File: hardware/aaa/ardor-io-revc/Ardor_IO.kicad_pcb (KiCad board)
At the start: 2 copper layers, 68 x 46 mm, 81 parts, among them J101 PI 40-PIN HEADER, J102 CODEC AUX L / GND / R, J202 TO MIDI PANEL / 4,5, J302 TO EXP PANEL / T,R,S, J502 TO YOUR AMP CIRCUIT, J503 TO LINE PANEL / T,S, K501 G5V-1 DC5, Q501 AO3400A, U201 H11L1M, U301 ADS1115IDGS, U401 TLV9002IDR, U402 TLV9002IDR

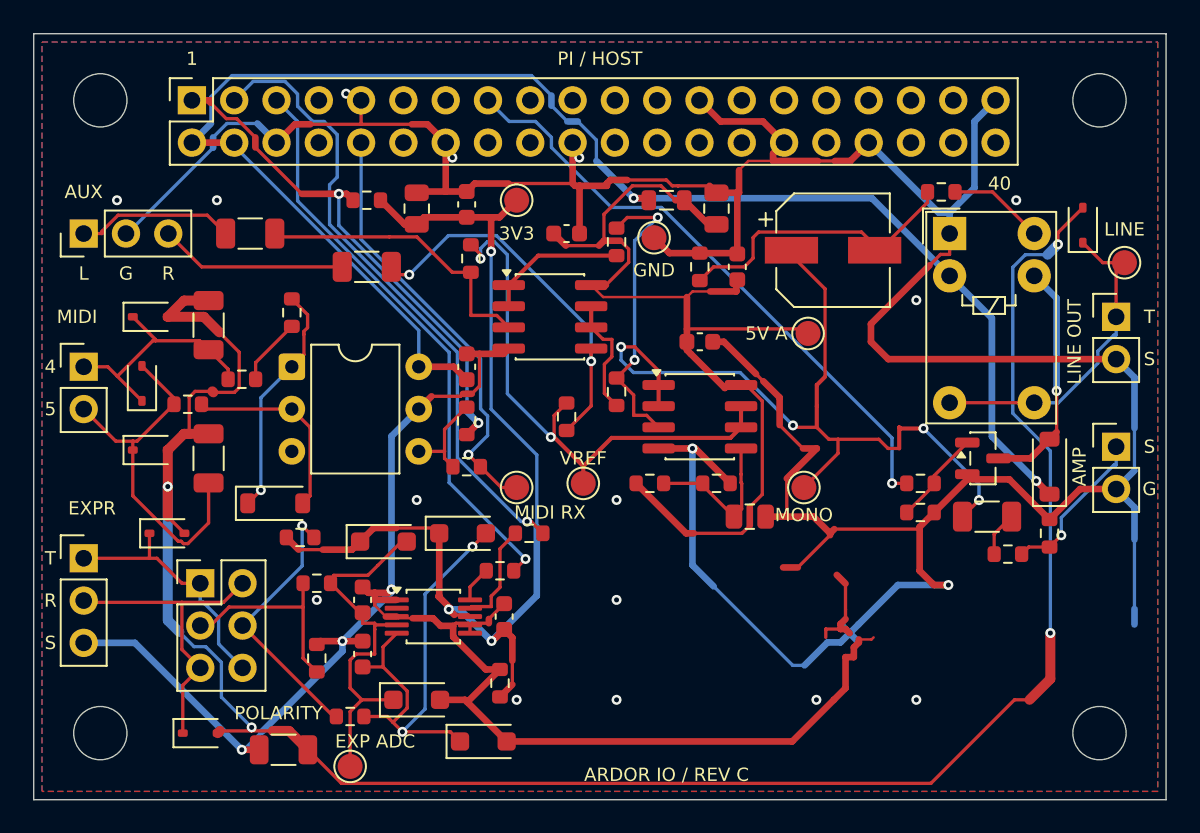
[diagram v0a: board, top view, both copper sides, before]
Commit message: fix: replace redundant Rev C ground tracks with copper pours
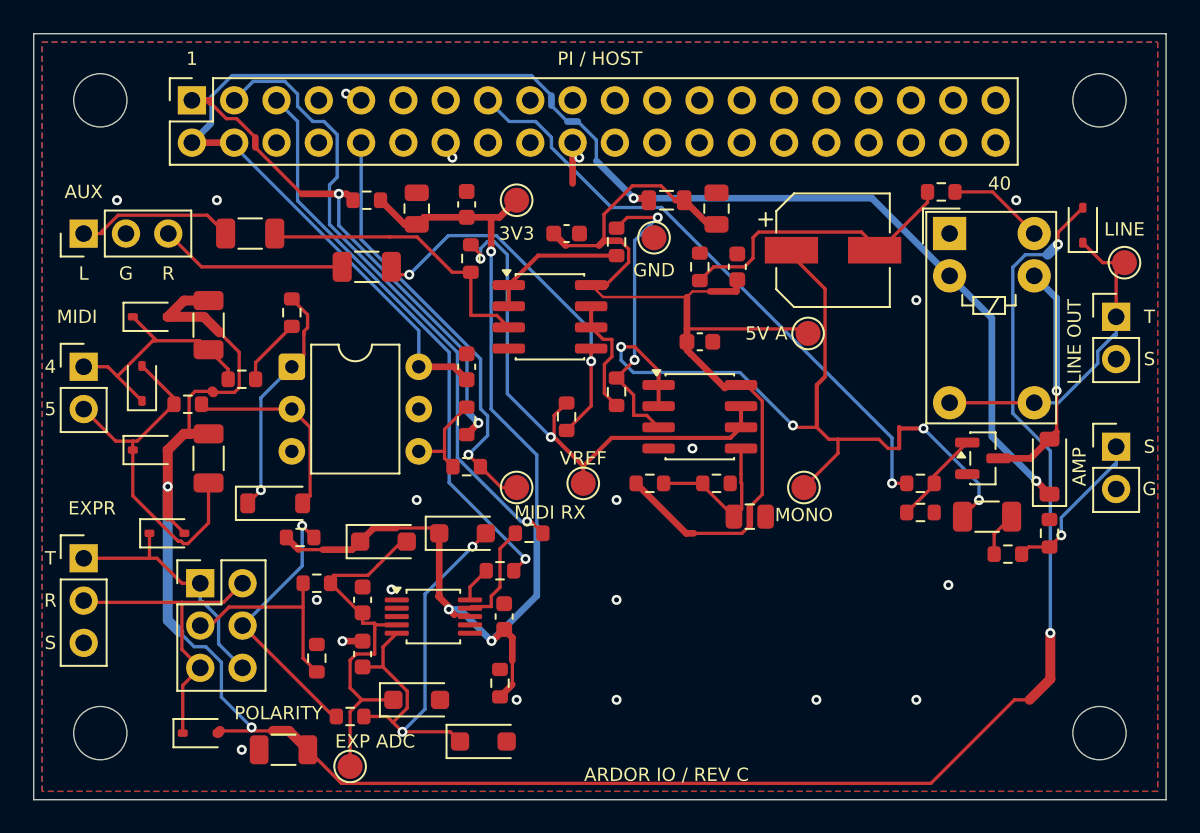
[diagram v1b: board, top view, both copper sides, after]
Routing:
- net GND: track 328.8 -> 4.65 mm
